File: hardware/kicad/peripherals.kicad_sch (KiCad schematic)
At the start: 31 parts, among them J301 IT8951 HAT, J302 Electrodes L, J303 Electrodes R, SW301 PEC11R-4220F-S0024, SW302 POWER, U301 CAP1188-1-CP-TR, U302 TPD2E2U06DCKR, U303 TPD2E2U06DCKR

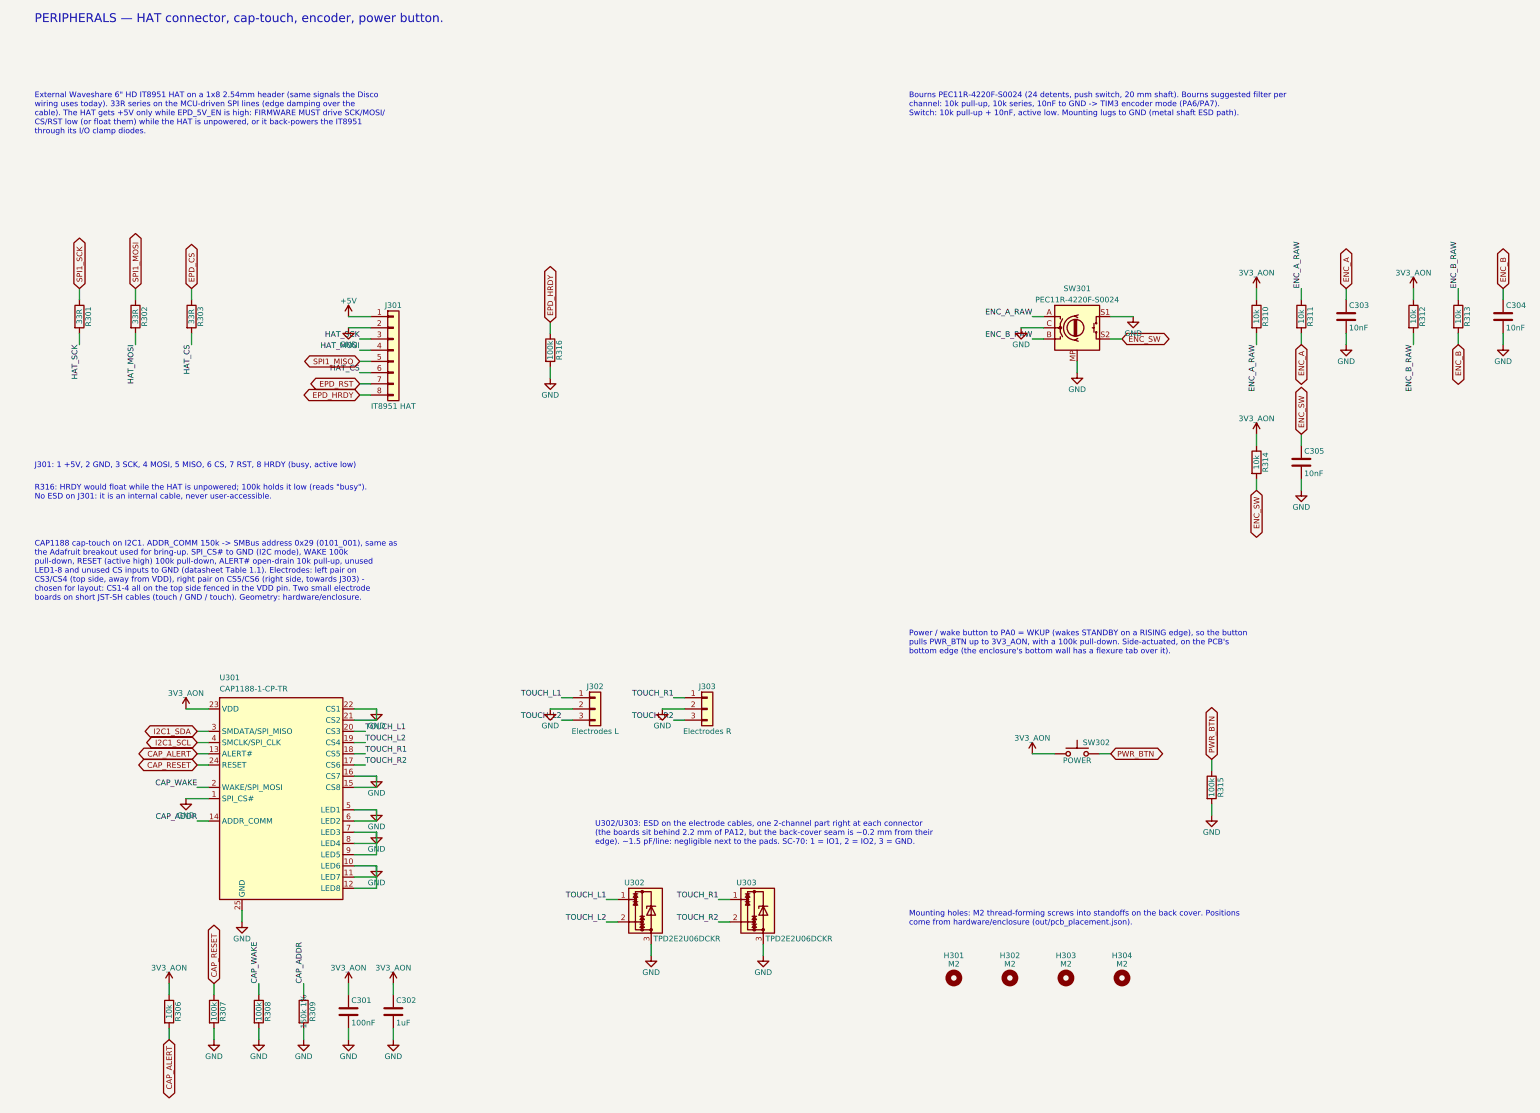
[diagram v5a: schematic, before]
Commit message: Schematic: Peripherals sheet redrawn with wired circuits
HAT header rows fan out to double pitch with the 33R series resistors
inline and the HRDY pull-down on its line; CAP1188 decoupling + ALERT#
pull-up on a 3V3_AON rail, RESET/WAKE/ADDR pull-downs and SPI_CS# on a GND
rail, unused CS/LED pins on one GND bus; electrode lines run to their
JST-SH connectors (drawn pins-down) with the ESD parts tapped on; encoder
A/B through the Bourns filter drawn in series, switch pull-up + cap; power
button pull-down wired. kicad_gen: label_at= for rotated multi-pin parts;
wiring.by_name shared. Electrically identical; board re-synced (0
unconnected, 0 parity issues).

Co-Authored-By: Claude Opus 5.5 <noreply@anthropic.com>
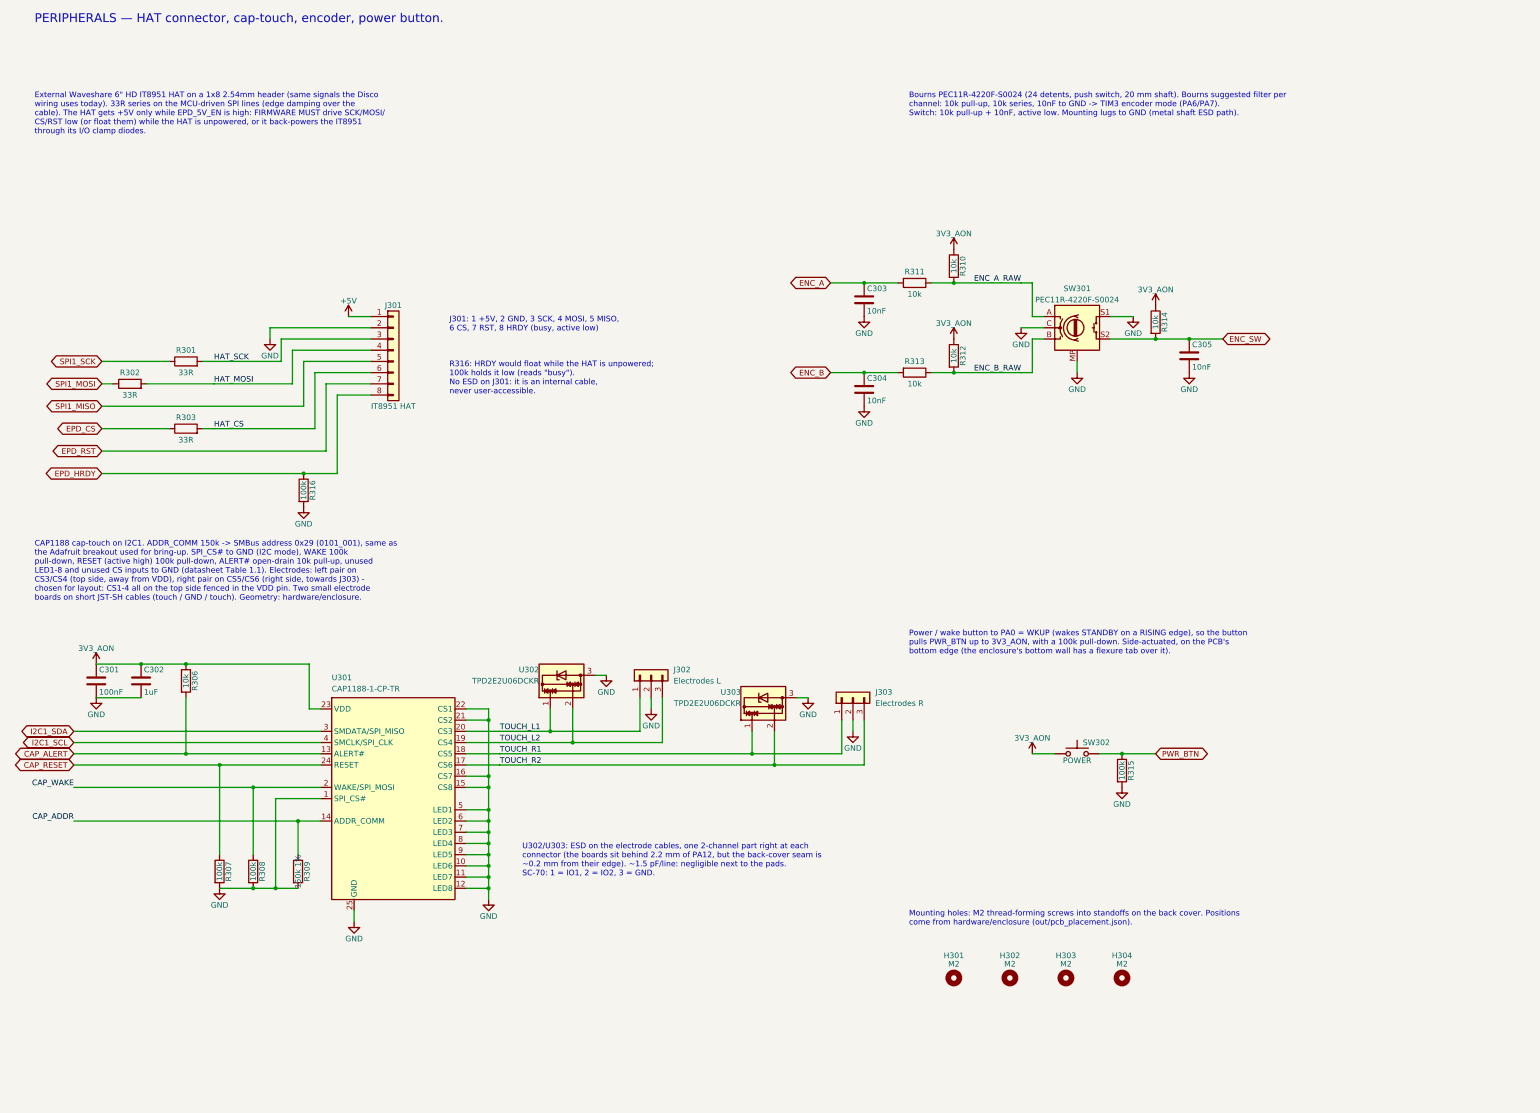
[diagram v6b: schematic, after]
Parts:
- removed R313: 10k, Resistor_SMD:R_0402_1005Metric, symbol Device:R
- added SW302: POWER, Button_Switch_SMD:SW_Push_1P1T-MP_NO_Horizontal_Alps_SKRTLAE010, symbol Switch:SW_Push
- R314: renamed from SW302; value POWER -> 10k; footprint Button_Switch_SMD:SW_Push_1P1T-MP_NO_Horizontal_Alps_SKRTLAE010 -> Resistor_SMD:R_0402_1005Metric; symbol Switch:SW_Push -> Device:R; MPN SKRTLAE010 -> (none)
- renumbered R314 to R313
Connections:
- net 3V3_AON: now also SW302.1; no longer R313.1
- net ENC_B: now also R313.2
- net ENC_B_RAW: now also R313.1
- net ENC_SW: now also R314.2; no longer R313.2
- net PWR_BTN: now also SW302.2; no longer R314.2
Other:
- moved on the sheet: R313
